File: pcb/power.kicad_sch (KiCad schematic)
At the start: 32 parts, among them J11 BM03B-SRSS-TB, J2 USB_C_USB2.0_16P, U2 LM66200DRLR, U3 USBLC6-2P6, U7 AZ1084-3.3

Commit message: Minor silkscreen changes.
Updated 2222 footprint
Ready for next release
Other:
- title: Aquarius Hub -> Aquarius Node
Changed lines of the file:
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@@
 	(paper "A4")
 	(title_block
-		(title "Aquarius Hub")
+		(title "Aquarius Node")
 		(date "<<release-date>>")
 		(rev "<<tag>>")
@@
 			)
 		)
-		(property "Datasheet" "https://optoelectronics.liteon.com/upload/download/DS22-2000-228/LTST-C191KGKT.PDF"
+		(property "Datasheet" "~"
 			(at 105.41 148.59 0)
 			(effects
@@
 			)
 		)
-		(property "Description" "20mA 315mcd Colorless Orange 120° 50mW 2.3V 0603"
+		(property "Description" "Light emitting diode, small symbol"
 			(at 105.41 148.59 0)
 			(effects
@@
 			)
 		)
+		(property "Sim.Pins" "1=K 2=A"
+			(at 105.41 148.59 0)
+			(effects
+				(font
+					(size 1.27 1.27)
+				)
+				(hide yes)
+			)
+		)
 		(pin "1"
 		)
@@
 			)
 		)
-		(property "Datasheet" "https://optoelectronics.liteon.com/upload/download/DS22-2000-228/LTST-C191KGKT.PDF"
+		(property "Datasheet" "~"
 			(at 118.11 148.59 0)
 			(effects
@@
 			)
 		)
-		(property "Description" "20mA 315mcd Colorless Orange 120° 50mW 2.3V 0603"
+		(property "Description" "Light emitting diode, small symbol"
 			(at 118.11 148.59 0)
 			(effects
@@
 			(effects
 				(font
+					(size 1.27 1.27)
+				)
+				(hide yes)
+			)
+		)
+		(property "Sim.Pins" "1=K 2=A"
+			(at 118.11 148.59 0)
+			(effects
+				(font

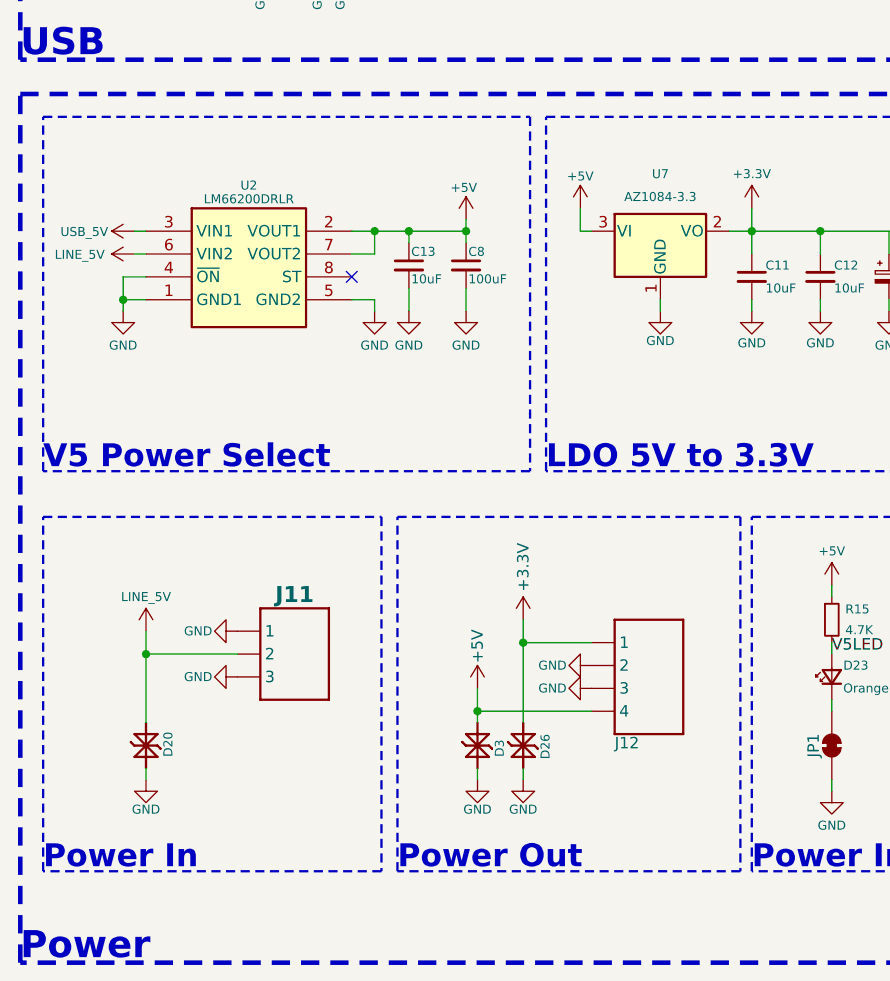
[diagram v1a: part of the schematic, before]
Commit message: Fixed part placement and missing model
Both display and 3.3 regulator were in the wrong place after updating from library!
LED was missing model
Minor silkscreen changes
Updated renders
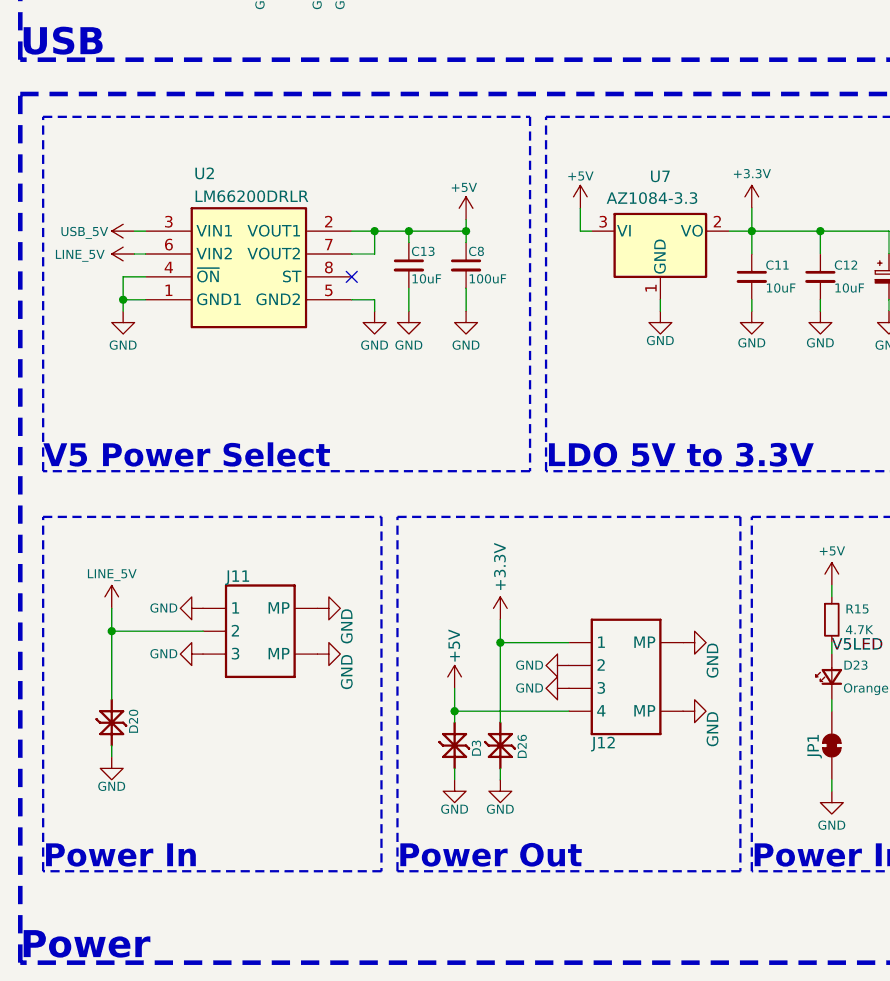
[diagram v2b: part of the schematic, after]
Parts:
- J11: value BM03B-SRSS-TB -> ~; LCSC C2904985 -> C2919601
- U7: footprint CRGM Power:TO-252-2 -> Package_TO_SOT_SMD:TO-252-2
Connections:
- net GND: now also J11.MP, J12.MP
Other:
- moved on the sheet: D20, D26, D3

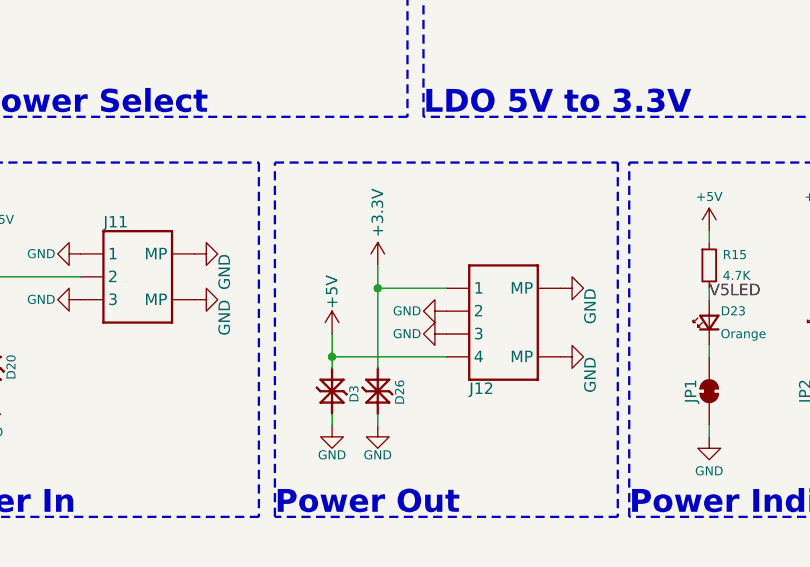
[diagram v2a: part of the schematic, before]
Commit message: Updated foot prints and symbols
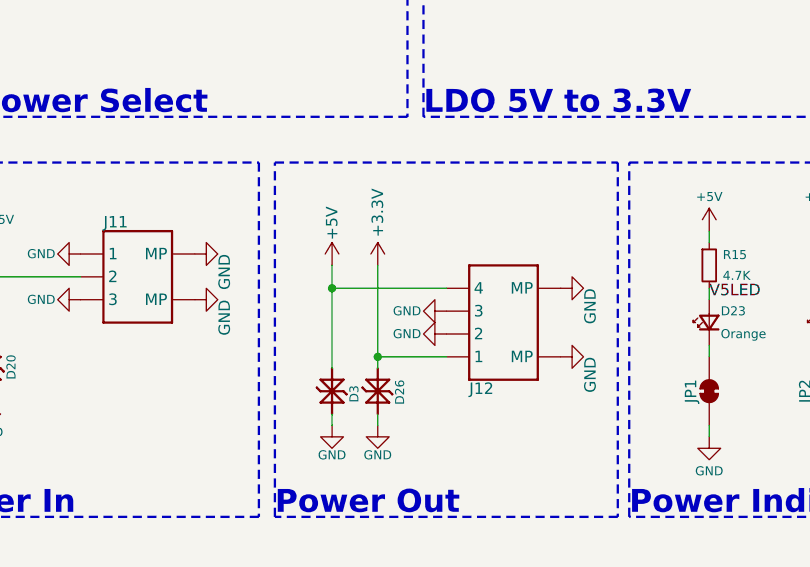
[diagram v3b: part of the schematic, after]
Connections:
- net GND: now also J11.0 (MP), J11.4 (MP), J12.0 (MP), J12.5 (MP); no longer J11.MP, J12.MP
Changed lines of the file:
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@@
 	)
 	(junction
+		(at 68.58 152.4)
+		(diameter 0)
+		(color 0 0 0 0)
+	)
+	(junction
 		(at 104.14 99.06)
 		(diameter 0)
@@
 	)
 	(junction
-		(at 26.67 106.68)
+		(at 63.5 144.78)
 		(diameter 0)
 		(color 0 0 0 0)
 	)
 	(junction
-		(at 63.5 152.4)
+		(at 26.67 106.68)
 		(diameter 0)
 		(color 0 0 0 0)
@@
 	)
 	(junction
-		(at 68.58 144.78)
-		(diameter 0)
-		(color 0 0 0 0)
-	)
-	(junction
 		(at 64.77 99.06)
 		(diameter 0)
@@
 	(wire
 		(pts
-			(xy 68.58 144.78) (xy 76.2 144.78)
-		)
-		(stroke
-			(width 0)
-			(type default)
-		)
-	)
-	(wire
-		(pts
 			(xy 64.77 48.26) (xy 68.58 48.26)
 		)
@@
 	(wire
 		(pts
-			(xy 68.58 144.78) (xy 68.58 142.24)
+			(xy 146.05 113.03) (xy 142.24 113.03)
 		)
 		(stroke
@@
 	(wire
 		(pts
-			(xy 146.05 113.03) (xy 142.24 113.03)
+			(xy 113.03 45.72) (xy 118.11 45.72)
 		)
 		(stroke
@@
 	(wire
 		(pts
-			(xy 113.03 45.72) (xy 118.11 45.72)
+			(xy 80.01 38.1) (xy 80.01 52.07)
 		)
 		(stroke
@@
 	(wire
 		(pts
-			(xy 80.01 38.1) (xy 80.01 52.07)
+			(xy 146.05 99.06) (xy 146.05 100.33)
 		)
 		(stroke
@@
 	(wire
 		(pts
-			(xy 146.05 99.06) (xy 146.05 100.33)
+			(xy 63.5 144.78) (xy 63.5 153.67)
 		)
 		(stroke
@@
 	(wire
 		(pts
-			(xy 63.5 149.86) (xy 63.5 152.4)
+			(xy 63.5 142.24) (xy 63.5 144.78)
 		)
 		(stroke
@@
 	(wire
 		(pts
+			(xy 68.58 152.4) (xy 76.2 152.4)
+		)
+		(stroke
+			(width 0)
+			(type default)
+		)
+	)
+	(wire
+		(pts
 			(xy 52.07 106.68) (xy 54.61 106.68)
 		)
@@
 	(wire
 		(pts
-			(xy 63.5 152.4) (xy 76.2 152.4)
-		)
-		(stroke
-			(width 0)
-			(type default)
-		)
-	)
-	(wire
-		(pts
 			(xy 64.77 35.56) (xy 87.63 35.56)
 		)
@@
 	(wire
 		(pts
-			(xy 105.41 161.29) (xy 105.41 160.02)
+			(xy 68.58 152.4) (xy 68.58 153.67)
 		)
 		(stroke
@@
 	(wire
 		(pts
-			(xy 29.21 106.68) (xy 26.67 106.68)
+			(xy 105.41 161.29) (xy 105.41 160.02)
 		)
 		(stroke
@@
 	(wire
 		(pts
-			(xy 82.55 33.02) (xy 95.25 33.02)
+			(xy 29.21 106.68) (xy 26.67 106.68)
 		)
 		(stroke
@@
 	(wire
 		(pts
-			(xy 123.19 33.02) (xy 123.19 40.64)
+			(xy 82.55 33.02) (xy 95.25 33.02)
 		)
 		(stroke
@@
 	(wire
 		(pts
-			(xy 63.5 152.4) (xy 63.5 153.67)
+			(xy 123.19 33.02) (xy 123.19 40.64)
 		)
 		(stroke
@@
 	(wire
 		(pts
-			(xy 68.58 144.78) (xy 68.58 153.67)
+			(xy 68.58 142.24) (xy 68.58 152.4)
 		)
 		(stroke
@@
 	(wire
 		(pts
+			(xy 63.5 144.78) (xy 76.2 144.78)
+		)
+		(stroke
+			(width 0)
+			(type default)
+		)
+	)
+	(wire
+		(pts
 			(xy 29.21 101.6) (xy 27.94 101.6)
 		)
@@
 		(pin "1"
 		)
-		(pin "MP"
+		(pin "0"
 		)
-		(pin "MP"
+		(pin "4"
 		)
 		(instances
@@
 		(pin "1"
 		)
-		(pin "MP"
+		(pin "5"
 		)
-		(pin "MP"
+		(pin "0"
 		)
 		(instances
@@
 	(symbol
 		(lib_id "power:+5V")
-		(at 63.5 149.86 0)
+		(at 63.5 142.24 0)
 		(unit 1)
 		(exclude_from_sim no)
@@
 		(dnp no)
 		(property "Reference" "#PWR045"
-			(at 63.5 153.67 0)
+			(at 63.5 146.05 0)
 			(effects
 				(font
@@
 		)
 		(property "Value" "+5V"
-			(at 63.5 147.066 90)
+			(at 63.5 139.446 90)
 			(effects
 				(font
@@
 		)
 		(property "Footprint" ""
-			(at 63.5 149.86 0)
+			(at 63.5 142.24 0)
 			(effects
 				(font
@@
 		)
 		(property "Datasheet" ""
-			(at 63.5 149.86 0)
+			(at 63.5 142.24 0)
 			(effects
 				(font
@@
 		)
 		(property "Description" "Power symbol creates a global label with name \"+5V\""
-			(at 63.5 149.86 0)
+			(at 63.5 142.24 0)
 			(effects
 				(font

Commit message: Updated footprints and rotations
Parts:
- U7: footprint Package_TO_SOT_SMD:TO-252-2 -> CRGM Power:TO-252-2
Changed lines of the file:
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@@
 			)
 		)
-		(property "Footprint" "Package_TO_SOT_SMD:TO-252-2"
+		(property "Footprint" "CRGM Power:TO-252-2"
 			(at 86.36 123.698 0)
 			(effects

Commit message: Fixed LCSC part # for power connector
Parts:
- J12: LCSC C2763614 -> C2919601
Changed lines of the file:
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@@
 			)
 		)
-		(property "LCSC" "C2763614"
+		(property "LCSC" "C2919601"
 			(at 82.042 117.856 0)
 			(effects

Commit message: Fixed part numbers
Fixed 3 pin JST LCSC Part Number
Fixed MPN for JST 3 pin
Changed Hub to Node on top silkscreen
Updated renders
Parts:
- J11: Digikey 455-BM04B-SRSS-TBTR-ND -> 455-BM03B-SRSS-TBTR-ND; LCSC C2919601 -> C2904985; MPN BM04B-SRSS-TB -> BM03B-SRSS-TB; Mouser 306-BM04BSRSSTBTLFSN -> 306-BM03BSRSSTBTLFSN
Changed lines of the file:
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@@
 			)
 		)
-		(property "LCSC" "C2919601"
+		(property "LCSC" "C2904985"
 			(at 38.1 177.546 0)
 			(effects
@@
 			)
 		)
-		(property "MPN" "BM04B-SRSS-TB"
+		(property "MPN" "BM03B-SRSS-TB"
 			(at 38.608 161.036 0)
 			(effects
@@
 			)
 		)
-		(property "Digikey" "455-BM04B-SRSS-TBTR-ND"
+		(property "Digikey" "455-BM03B-SRSS-TBTR-ND"
 			(at 38.1 172.974 0)
 			(effects
@@
 			)
 		)
-		(property "Mouser" "306-BM04BSRSSTBTLFSN"
+		(property "Mouser" "306-BM03BSRSSTBTLFSN"
 			(at 38.1 175.514 0)
 			(effects

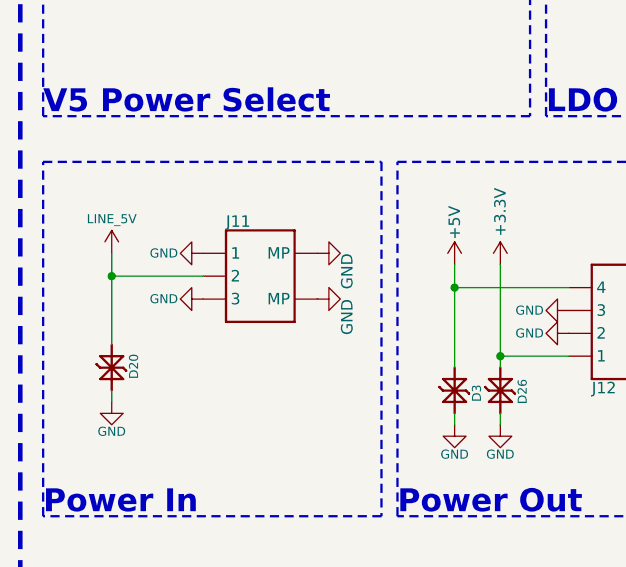
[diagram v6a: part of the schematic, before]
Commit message: Added analog port
re-routed
resized the pretty princess
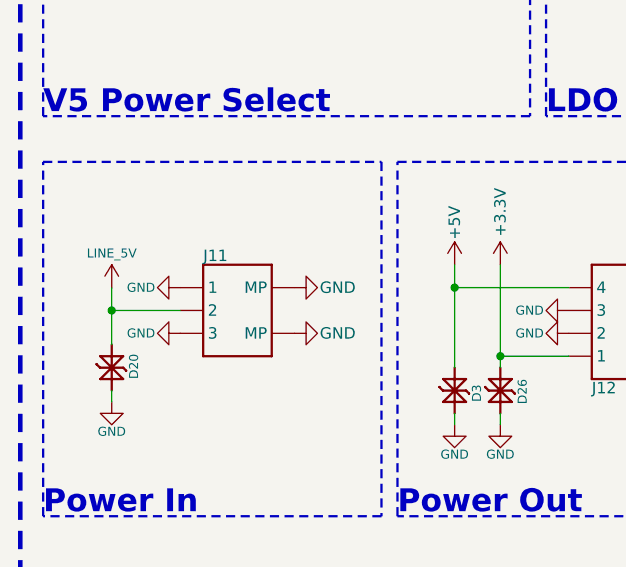
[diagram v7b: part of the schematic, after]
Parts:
- J11: Digikey 455-BM03B-SRSS-TBTR-ND -> 455-BM04B-SRSS-TBTR-ND; LCSC C2904985 -> C2919601; MPN BM03B-SRSS-TB -> BM04B-SRSS-TB; Mouser 306-BM03BSRSSTBTLFSN -> 306-BM04BSRSSTBTLFSN
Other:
- moved on the sheet: J11
